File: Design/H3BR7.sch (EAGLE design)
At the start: 62 parts, among them P2 HEXABIT_X2_P1_P5, Q10 MMBT3904LT1, Q11 MMBT3904LT1, Q12 MMBT3904LT1, Q13 MMBT3904LT1, Q14 MMBT3904LT1, Q7 MMBT3904LT1, Q8 MMBT3904LT1, Q9 MMBT3904LT1, U1 STM32G0B1CEU6N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

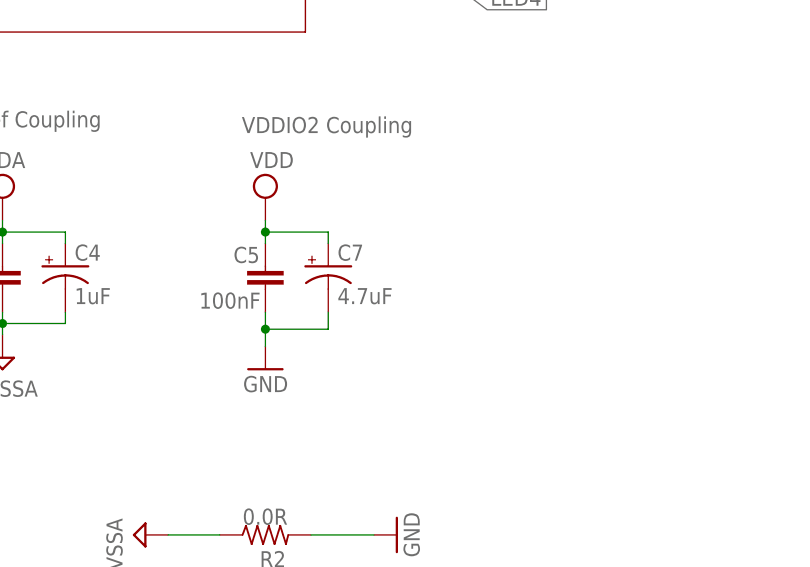
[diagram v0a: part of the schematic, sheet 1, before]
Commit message: -Add Tvs diode -Update the LOGO -Fix the clearance and soldermask  layer issues
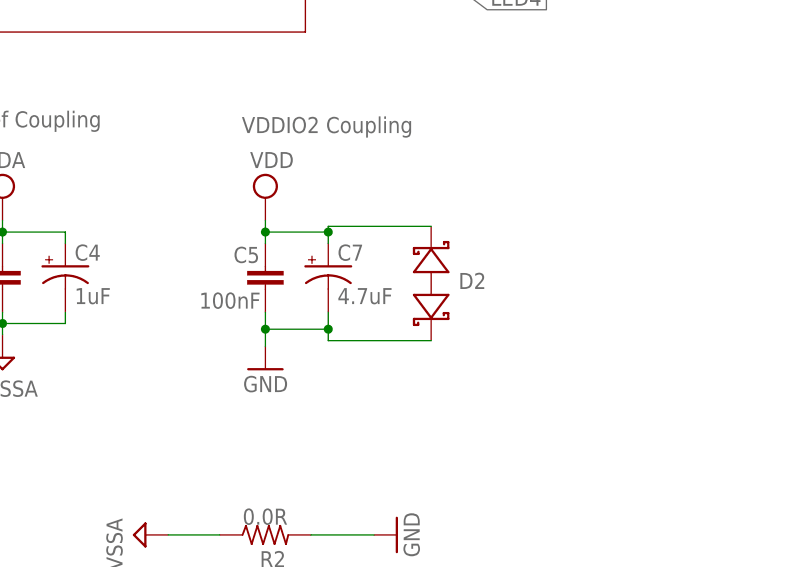
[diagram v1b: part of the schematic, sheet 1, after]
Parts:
- added D2: BOURNS_CDSOD323-T03SCBOURNS_CDSOD323-T03SC_0_0, HEXABITZ_RCLS:BOURNS_CDSOD323-T03SCBOURNS_CDSOD323-T03SC_0_0
- added TRIMBLE-LOGO1: HEXA-LOGO, HEXABITZ_USER_INTERFACE_PARTS:HEXA-LOGO
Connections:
- net GND: now also D2.A
- net VDD: now also D2.C
